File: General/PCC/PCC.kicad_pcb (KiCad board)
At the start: 2 copper layers, 23.5 x 52.5 mm, 24 parts, among them J1 Conn_01x03, SW1 SW_DIP_x04, U1 I6A4W020A033V-001-R

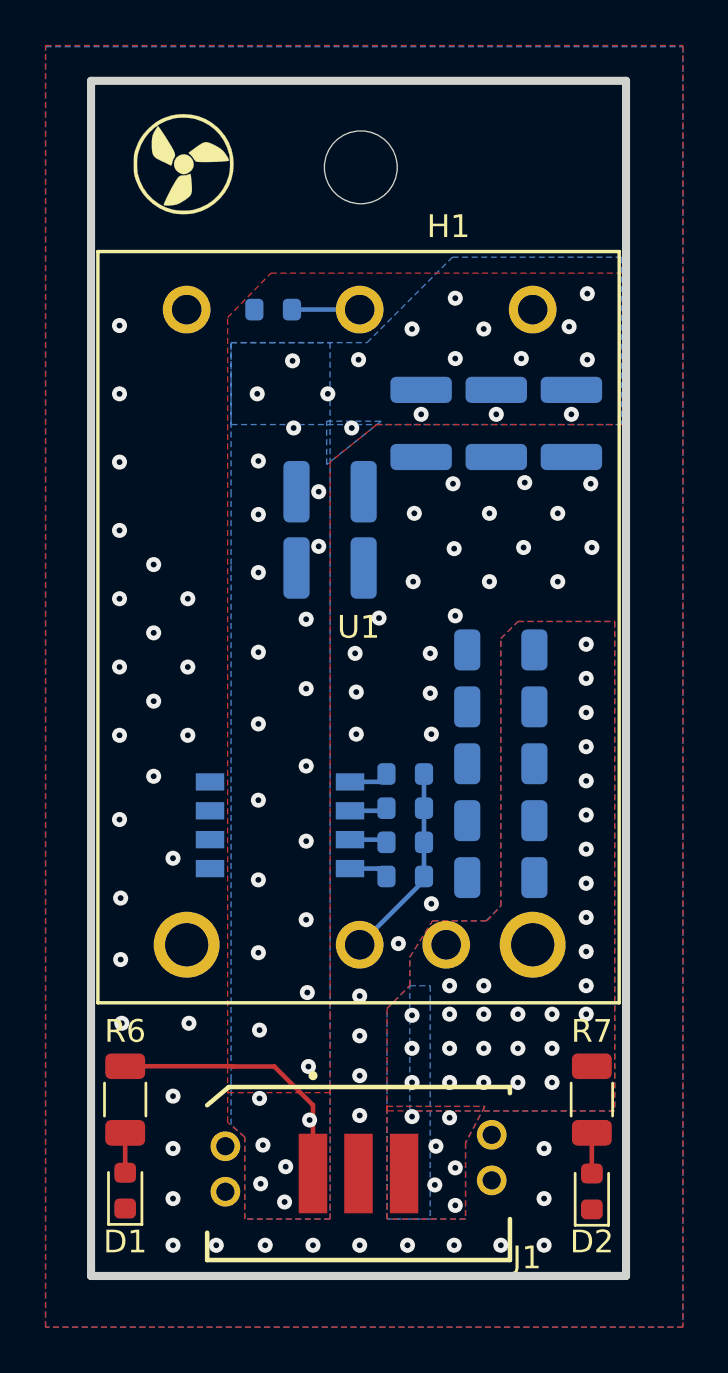
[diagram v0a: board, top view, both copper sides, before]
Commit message: updated layout
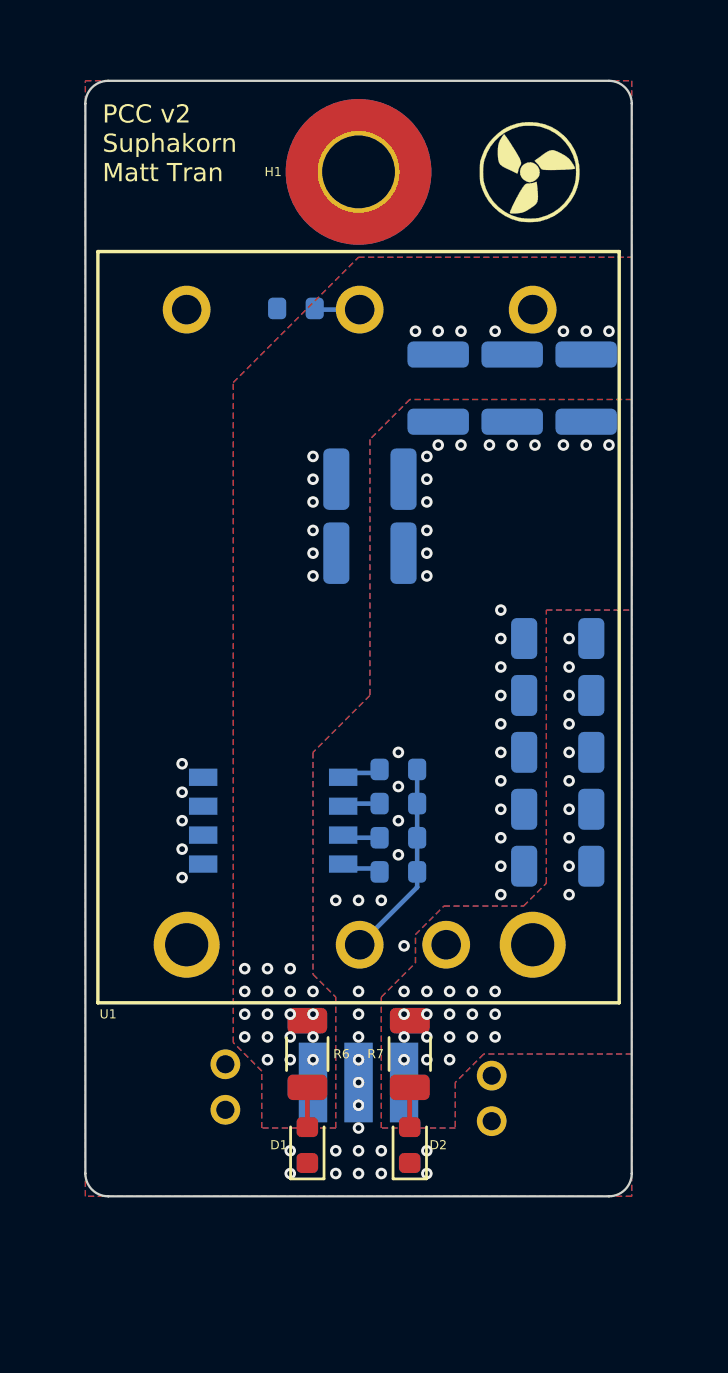
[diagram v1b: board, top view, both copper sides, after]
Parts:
- removed G***: LOGO, extraparts:auv_logo
- added H2: logo, extraparts:auv_logo, F.Cu at (157.5, 80.0)
- H1: value MountingHole -> mount; footprint MountingHole:MountingHole_3.2mm_M3 -> MountingHole:MountingHole_3.2mm_M3_Pad_TopBottom
- J1: value Conn_01x03 -> PWR; moved to B.Cu
- moved C10 10.8 mm to (158.8, 100.5)
- moved C6 9.82 mm to (158.8, 110.5)
- moved D2 8.26 mm to (152.2, 122.8)
- moved D1 8.25 mm to (147.8, 122.8)
- moved R6 8.25 mm to (147.8, 118.8)
- moved R7 8.25 mm to (152.2, 118.8)
- moved C9 6.04 mm to (158.8, 103.0)
- moved C7 5.15 mm to (158.8, 108.0)
- moved C2 4.27 mm to (150.5, 93.5)
- moved J1 4.00 mm to (150.0, 120.0)
- moved C1 3.22 mm to (150.5, 96.8)
- moved C8 2.55 mm to (158.8, 105.5)
- moved C3 1.72 mm to (153.5, 89.5)
- moved C4 1.70 mm to (156.8, 89.5)
- moved C5 1.68 mm to (160.0, 89.5)
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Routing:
- net +48V: track 12.0 -> 0.00 mm, vias 41 -> 31
- net Net-(R1-Pad2): track 2.98 -> 2.00 mm
- net GND: vias 60 -> 55
- net +VSW: vias 35 -> 28
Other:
- board size 23.5 x 52.5 mm -> 24 x 49 mm
- board text added: "3V3 5V 12V 15V"
- board text added: "PCC v2 Suphakorn Matt Tran"
- board text added: "Vout|GND|Vin"
- board text removed: "3v3 5v 12v 15v"
- board text removed: "PCB v2 by Suphakorn"
